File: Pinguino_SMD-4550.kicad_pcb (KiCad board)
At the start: 2 copper layers, 120 x 40 mm, 50 parts, among them P1 uUSB, P10 CONN_01X01, P11 CONN_01X01, P12 CONN_01X01, P13 CONN_01X01, P14 CONN_01X01, P15 CONN_01X01, P16 CONN_01X01, P17 CONN_01X01, P18 CONN_01X01, P19 CONN_01X01, P2 CONN_01X01, P20 CONN_01X01, P21 CONN_01X01, P22 CONN_01X01, P23 CONN_01X01, P24 CONN_01X01, P25 CONN_01X01, P26 CONN_01X01, P27 CONN_01X01, P28 CONN_01X01, P29 CONN_01X01, P3 CONN_01X01, P30 CONN_01X01, P31 CONN_01X01, P32 CONN_01X01, P33 CONN_01X01, P34 CONN_01X01, P35 CONN_01X01, P36 CONN_01X01, P37 CONN_01X01, P4 CONN_01X01, P5 CONN_01X01, P6 CONN_01X01, P7 CONN_01X01, P8 CONN_01X01, P9 CONN_01X01, SW1 Reset, U1 PIC18(L)F4550-I/PT, Y1 Crystal

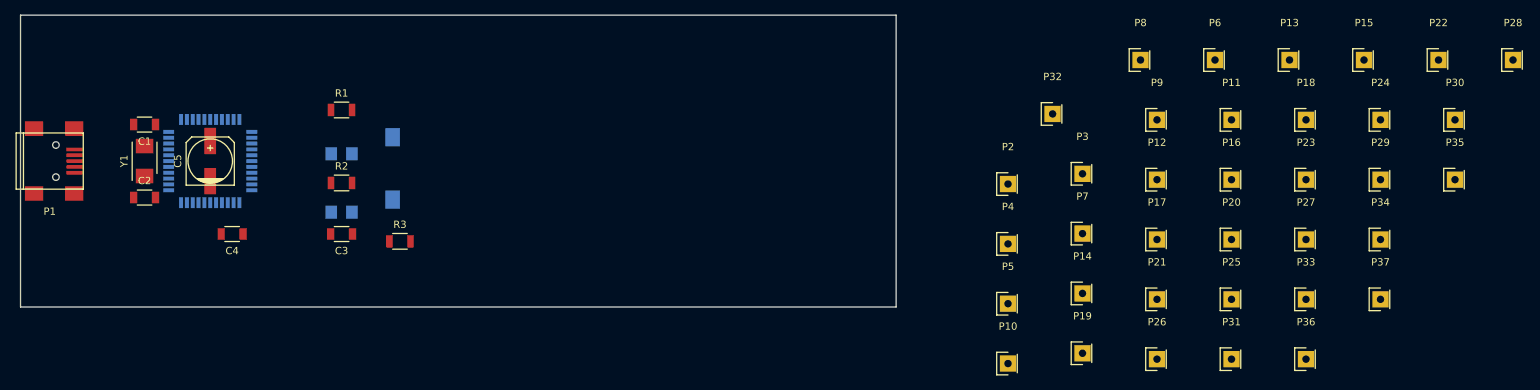
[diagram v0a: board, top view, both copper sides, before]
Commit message: Reorganized and aligned components. Capapol -> Tantalum B 3528.
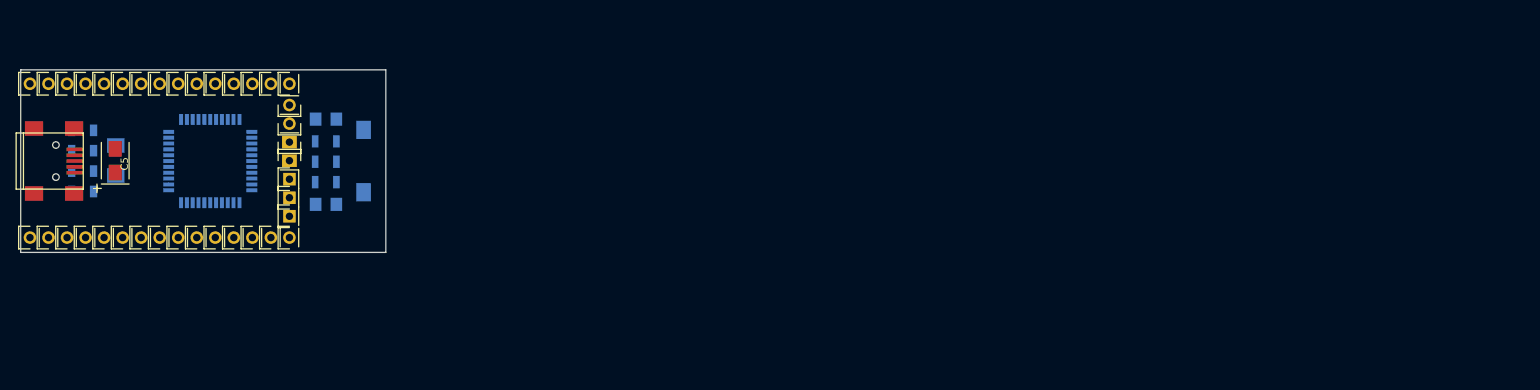
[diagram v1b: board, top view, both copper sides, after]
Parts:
- added P38: CONN_01X01, Socket_Strips:Socket_Strip_Straight_1x01, F.Cu at (101.9, 67.6)
- C1, C2, C3, C4, R1, R2, R3, Y1: moved to B.Cu
- C5: footprint Capacitors_SMD:c_elec_6.3x5.3 -> Capacitors_Tantalum_SMD:TantalC_SizeB_EIA-3528_Wave
- moved P28 197.1 mm to (73.9, 70.5)
- moved P30 190.9 mm to (71.4, 70.5)
- moved P34 185.1 mm to (66.3, 70.5)
- moved P37 177.4 mm to (76.5, 49.4)
- moved P22 174.4 mm to (86.6, 70.5)
- moved P24 168.1 mm to (84.1, 70.5)
- moved P36 166.5 mm to (79.0, 49.4)
- moved P15 165.1 mm to (84.1, 49.4)
- moved P35 165.0 mm to (96.8, 70.5)
- moved P23 164.9 mm to (76.5, 70.5)
- moved P6 162.4 mm to (66.3, 49.4)
- moved P29 159.9 mm to (91.7, 70.5)
- moved P13 157.4 mm to (81.5, 49.4)
- moved P11 157.1 mm to (73.9, 49.4)
- moved P33 149.9 mm to (94.2, 49.4)
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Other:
- board size 120 x 40 mm -> 50 x 25 mm
- net class Default: clearance 0.2 -> 0.3048; trace_width 0.25 -> 0.3048; via_dia 0.6 -> 0.889; via_drill 0.4 -> 0.635
- net class Power added: clearance 0.4318, trace_width 0.4318, via_dia 1.397, via_drill 1.016
- rule trace_clearance: 0.2 -> 0.3048
- rule trace_min: 0.2 -> 0.1524
- rule via_min_drill: 0.3 -> 0.3302

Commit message: Autoruting
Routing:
- net GND: track 0.00 -> 87.3 mm, vias 0 -> 1
- net VCC: track 0.00 -> 65.9 mm, vias 0 -> 2
- net /VUSB: track 0.00 -> 35.0 mm, vias 0 -> 2
- net /MCLR: track 0.00 -> 32.7 mm, vias 0 -> 2
- net Net-(C3-Pad2): track 0.00 -> 27.2 mm, vias 0 -> 2
- net /OSC1: track 0.00 -> 23.9 mm, vias 0 -> 2
- net /PIN28: track 0.00 -> 23.0 mm
- net /PIN0/SDA: track 0.00 -> 22.7 mm
- net /OSC0: track 0.00 -> 22.6 mm, vias 0 -> 2
- net Net-(P1-Pad5): track 0.00 -> 22.5 mm
- net /D-: track 0.00 -> 21.1 mm, vias 0 -> 1
- net /PIN27: track 0.00 -> 20.1 mm
- net /RA4: track 0.00 -> 20.0 mm
- net /PIN1/SCL: track 0.00 -> 19.9 mm
- net /D+: track 0.00 -> 19.1 mm, vias 0 -> 1
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
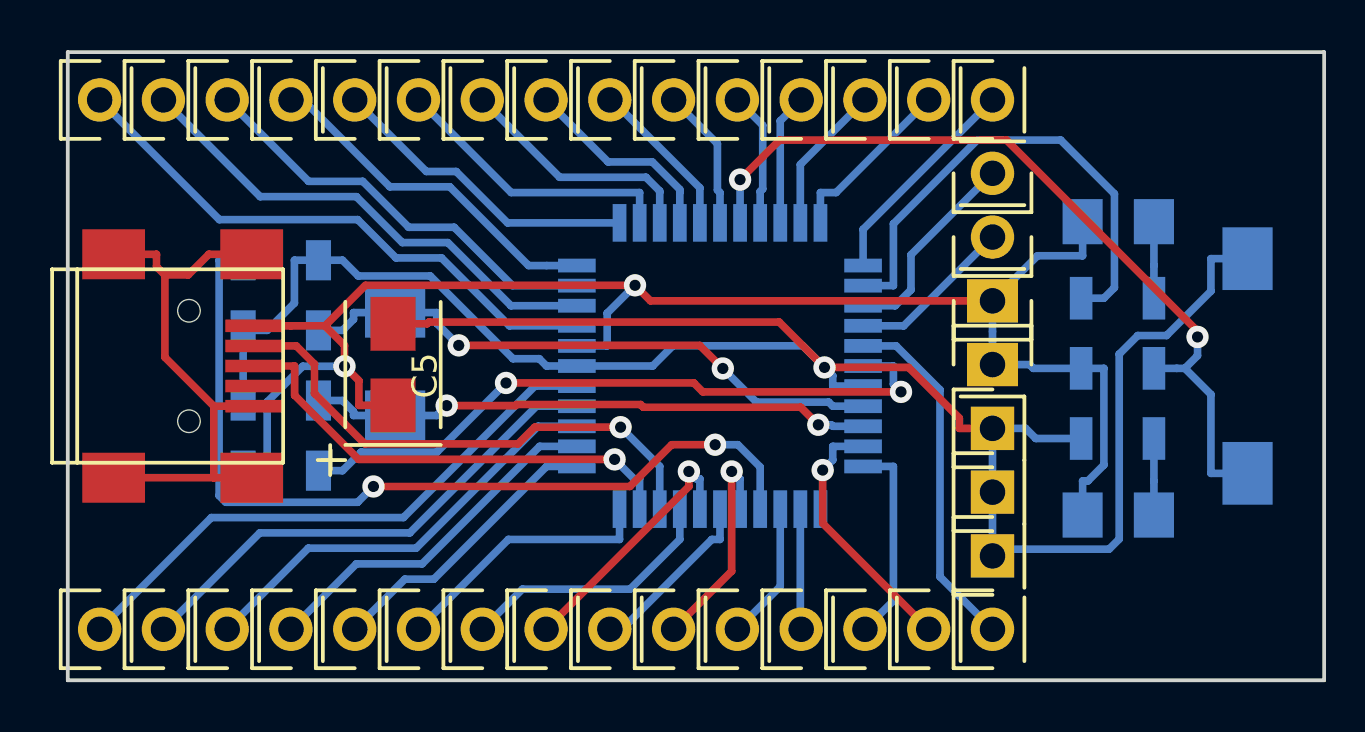
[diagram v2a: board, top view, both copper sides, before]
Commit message: Fixed error: VCC -> Pin 28, GND -> C3. Autoruting
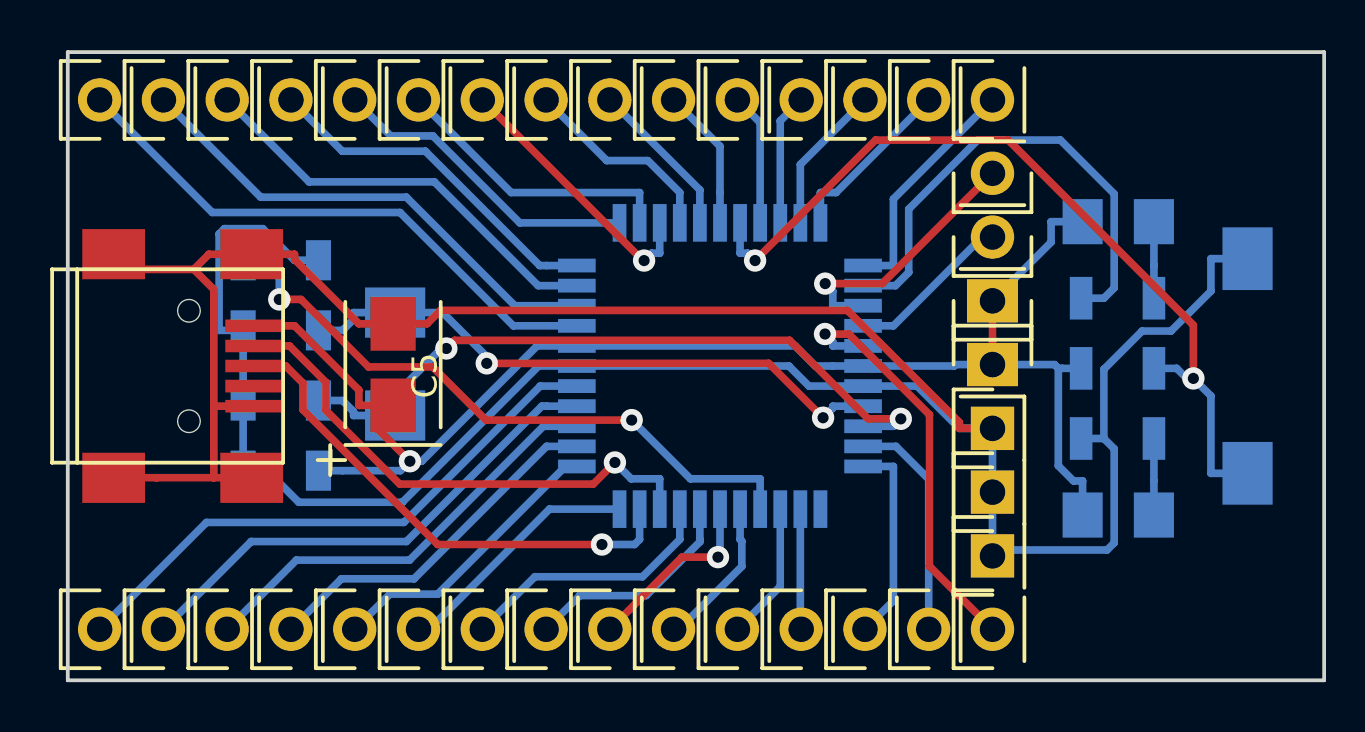
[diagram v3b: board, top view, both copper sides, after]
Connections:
- C3 pad 1: VCC -> GND
- C3 pad 2: Net-(C3-Pad2) -> VCC
- P1 pad 5: Net-(P1-Pad5) -> GND
- P1 pad 6: Net-(P1-Pad5) -> GND
- U1 pad 28: Net-(C3-Pad2) -> VCC
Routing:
- net GND: track 87.3 -> 130.1 mm, vias 1 -> 0
- net Net-(C3-Pad2): track 27.2 -> 0.00 mm, vias 2 -> 0
- net Net-(P1-Pad5): track 22.5 -> 0.00 mm
- net /VUSB: track 35.0 -> 26.0 mm
- net VCC: track 65.9 -> 57.2 mm, vias 2 -> 1
- net /OSC0: track 22.6 -> 28.5 mm
- net /PIN21: track 8.91 -> 6.07 mm, vias 1 -> 0
- net /PIN20/A7: track 14.2 -> 16.9 mm, vias 0 -> 1
- net /PIN18/A5: track 8.16 -> 10.7 mm, vias 0 -> 1
- net /PIN23: track 10.4 -> 8.87 mm, vias 1 -> 0
- net /PIN10: track 10.4 -> 9.13 mm, vias 1 -> 0
- net /PIN4: track 9.84 -> 11.0 mm, vias 0 -> 1
- net /D+: track 19.1 -> 20.2 mm
- net /MCLR: track 32.7 -> 33.8 mm
- net /PIN8/TX: track 10.7 -> 9.99 mm
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
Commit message: Tracks improvement
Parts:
- added 2.2mm: MountingHole_2.2mm_M2_DIN965, Mounting_Holes:MountingHole_2.2mm_M2_DIN965, F.Cu at (112.3, 50.3)
- added REF**: MountingHole_2.2mm_M2_DIN965, Mounting_Holes:MountingHole_2.2mm_M2_DIN965, F.Cu at (112.3, 69.7)
- added REF**: MountingHole_2.2mm_M2_DIN965, Mounting_Holes:MountingHole_2.2mm_M2_DIN965, F.Cu at (66.8, 52.5)
- added REF**: MountingHole_2.2mm_M2_DIN965, Mounting_Holes:MountingHole_2.2mm_M2_DIN965, F.Cu at (66.8, 67.6)
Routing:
- net GND: track 130.1 -> 136.4 mm
- net /OSC1: track 24.3 -> 28.8 mm
- net VCC: track 57.2 -> 60.2 mm
- net /PIN18/A5: track 10.7 -> 8.20 mm, vias 1 -> 0
- net /ICSP-VPP: track 8.16 -> 6.52 mm
- net /D-: track 20.9 -> 22.5 mm
- net /PIN27: track 20.1 -> 21.5 mm
- net /PIN22: track 7.44 -> 8.75 mm, vias 1 -> 0
- net /PIN4: track 11.0 -> 9.81 mm, vias 1 -> 0
- net /D+: track 20.2 -> 21.1 mm
- net /PIN0/SDA: track 22.7 -> 23.4 mm
- net /MCLR: track 33.8 -> 33.3 mm
- net /PIN9/RX: track 11.5 -> 12.0 mm
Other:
- board size 50 x 25 mm -> 50.8 x 25 mm

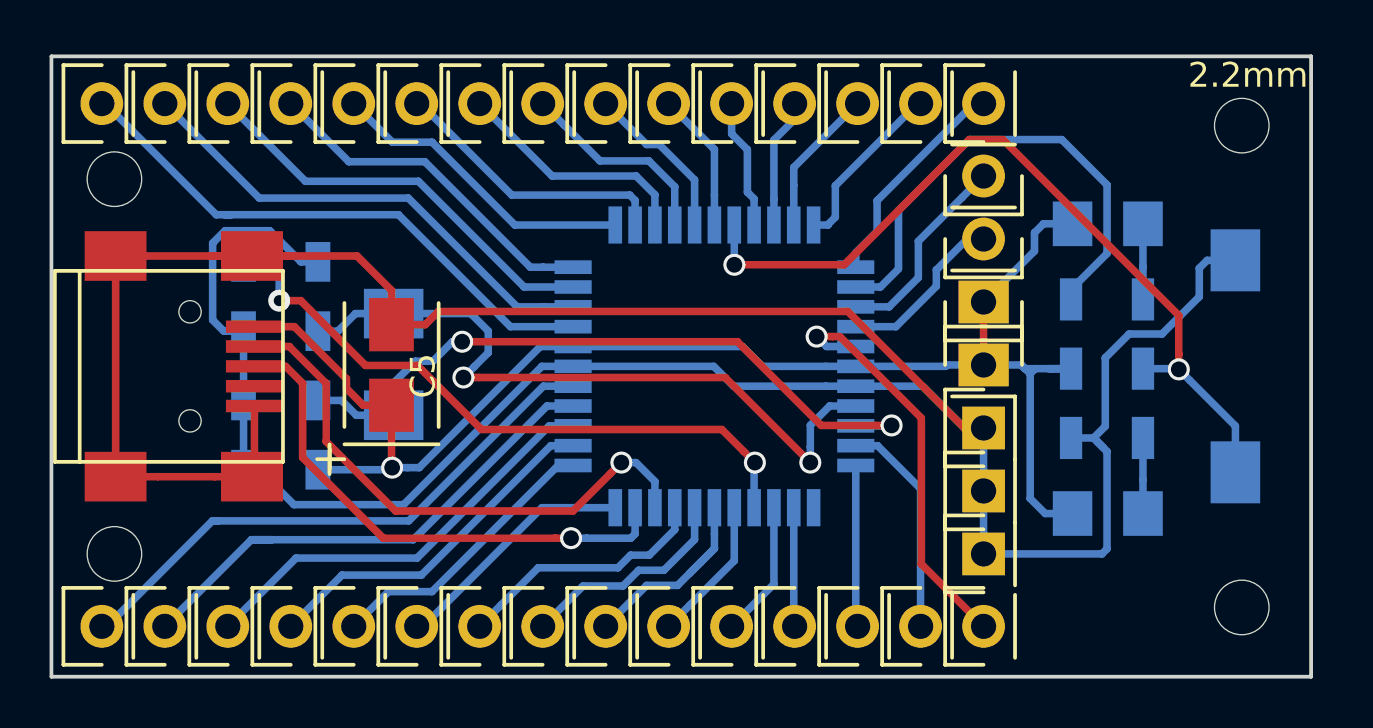
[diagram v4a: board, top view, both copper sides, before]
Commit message: Added zones (F.cu, B.cu)
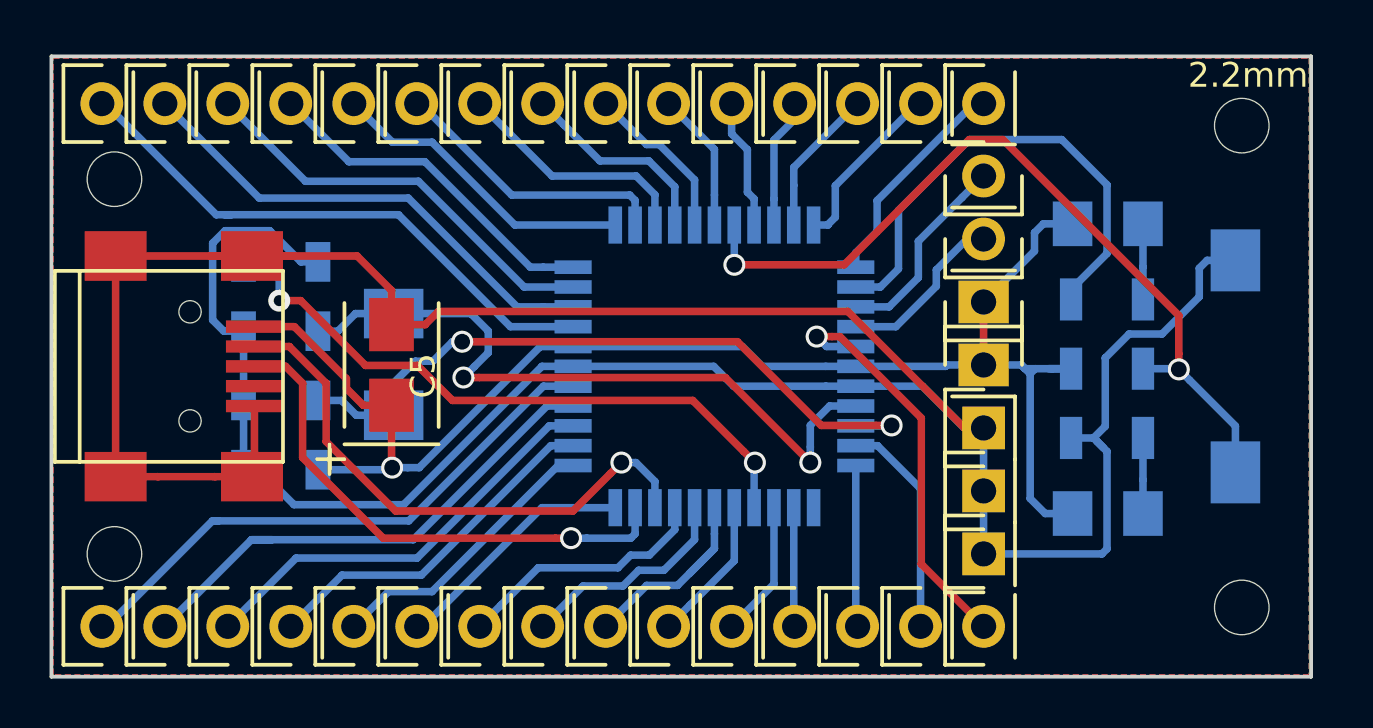
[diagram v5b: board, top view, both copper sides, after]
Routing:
- added copper zone on B.Cu, net GND
- added copper zone on F.Cu, net GND
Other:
- net class Power: clearance 0.4318 -> 0.3048
- rule trace_min: 0.1524 -> 0.3048
- rule via_min_size: 0.4 -> 0.381
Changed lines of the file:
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@@
     (links 69)
     (no_connects 0)
-    (area 64.186999 47.422999 115.137001 72.592001)
+    (area 52.960001 42.87 125.076372 73.7028)
     (thickness 1.6)
     (drawings 7)
@@
     (34 B.Paste user)
     (35 F.Paste user)
-    (36 B.SilkS user hide)
-    (37 F.SilkS user hide)
-    (38 B.Mask user hide)
-    (39 F.Mask user hide)
+    (36 B.SilkS user)
+    (37 F.SilkS user)
+    (38 B.Mask user)
+    (39 F.Mask user)
     (40 Dwgs.User user)
     (41 Cmts.User user)
@@
     (user_trace_width 0.8128)
     (trace_clearance 0.3048)
-    (zone_clearance 0.508)
+    (zone_clearance 0.254)
     (zone_45_only no)
-    (trace_min 0.1524)
+    (trace_min 0.3048)
     (segment_width 0.2)
     (edge_width 0.15)
     (via_size 0.889)
     (via_drill 0.635)
-    (via_min_size 0.4)
+    (via_min_size 0.381)
     (via_min_drill 0.3302)
     (user_via 0.508 0.3302)
@@
     (uvia_drill 0.127)
     (uvias_allowed no)
-    (uvia_min_size 0.2)
-    (uvia_min_drill 0.1)
+    (uvia_min_size 0)
+    (uvia_min_drill 0)
     (pcb_text_width 0.3)
     (pcb_text_size 1.5 1.5)
@@
     (visible_elements FFFFFF7F)
     (pcbplotparams
-      (layerselection 0x00030_80000001)
+      (layerselection 0x000f0_80000001)
       (usegerberextensions false)
       (excludeedgelayer true)
@@
   )
   (net_class Power ""
-    (clearance 0.4318)
+    (clearance 0.3048)
     (trace_width 0.4318)
     (via_dia 1.397)
@@
   (segment (start 101.854 59.944) (end 100.3805 59.944) (width 0.3048) (layer B.Cu) (net 4))
   (segment (start 101.854 59.944) (end 101.854 57.404) (width 0.3048) (layer F.Cu) (net 4))
-  (segment (start 81.608015 62.546922) (end 91.297155 62.546922) (width 0.3048) (layer F.Cu) (net 5))
+  (segment (start 92.187553 63.43732) (end 92.632052 63.881819) (width 0.3048) (layer F.Cu) (net 5))
+  (segment (start 90.124815 61.374582) (end 92.187553 63.43732) (width 0.3048) (layer F.Cu) (net 5))
+  (segment (start 80.435675 61.374582) (end 90.124815 61.374582) (width 0.3048) (layer F.Cu) (net 5))
+  (segment (start 79.023647 59.962554) (end 80.435675 61.374582) (width 0.3048) (layer F.Cu) (net 5))
+  (segment (start 73.4485 57.3495) (end 74.3146 57.3495) (width 0.3048) (layer F.Cu) (net 5))
   (segment (start 76.927654 59.962554) (end 79.023647 59.962554) (width 0.3048) (layer F.Cu) (net 5))
   (segment (start 74.3146 57.3495) (end 76.927654 59.962554) (width 0.3048) (layer F.Cu) (net 5))
-  (segment (start 79.023647 59.962554) (end 81.608015 62.546922) (width 0.3048) (layer F.Cu) (net 5))
-  (segment (start 91.297155 62.546922) (end 92.187553 63.43732) (width 0.3048) (layer F.Cu) (net 5))
-  (segment (start 73.4485 57.3495) (end 74.3146 57.3495) (width 0.3048) (layer F.Cu) (net 5))
-  (segment (start 92.187553 63.43732) (end 92.632052 63.881819) (width 0.3048) (layer F.Cu) (net 5))
   (segment (start 92.6 63.913871) (end 92.632052 63.881819) (width 0.3048) (layer B.Cu) (net 5))
   (segment (start 92.6 65.7) (end 92.6 63.913871) (width 0.3048) (layer B.Cu) (net 5))
@@
   (segment (start 91.8 54.3) (end 91.8 55.900097) (width 0.3048) (layer B.Cu) (net 43))
   (via (at 91.80339 55.903487) (size 0.889) (drill 0.635) (layers F.Cu B.Cu) (net 43))
+  (zone (net 1) (net_name GND) (layer F.Cu) (hatch edge 0.508)
+    (connect_pads (clearance 0.3048))
+    (min_thickness 0.3048)
+    (fill yes (arc_segments 16) (thermal_gap 0.3048) (thermal_bridge_width 0.381) (smoothing fillet))
+    (polygon
+      (pts
+        (xy 64.3382 47.5742) (xy 114.9858 47.5742) (xy 114.9858 72.4408) (xy 64.3382 72.4408)
+      )
+    )
+  )
+  (zone (net 1) (net_name GND) (layer B.Cu) (hatch edge 0.508)
+    (connect_pads (clearance 0.254))
+    (min_thickness 0.254)
+    (fill yes (arc_segments 16) (thermal_gap 0.254) (thermal_bridge_width 0.381) (smoothing fillet))
+    (polygon
+      (pts
+        (xy 114.9858 72.4408) (xy 64.3382 72.4408) (xy 64.3382 47.5742) (xy 114.9858 47.5742) (xy 114.9858 72.4408)
+      )
+    )
+  )
 )
